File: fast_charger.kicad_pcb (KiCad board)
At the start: 2 copper layers, 71.1 x 38.7 mm, 47 parts, among them J1 Screw_Terminal_01x02, J2 USB_A, J3 AVR-ISP-6, J4 Conn_02x08_Odd_Even, J5 Conn_02x03_Odd_Even, Q1 PJD25N03, Q2 PJD25N03, U1 CHY100, U2 IRS10752LVBF, U3 ATtiny404-SS, U4 AP7375, U5 AP7375, U6 INA180A4

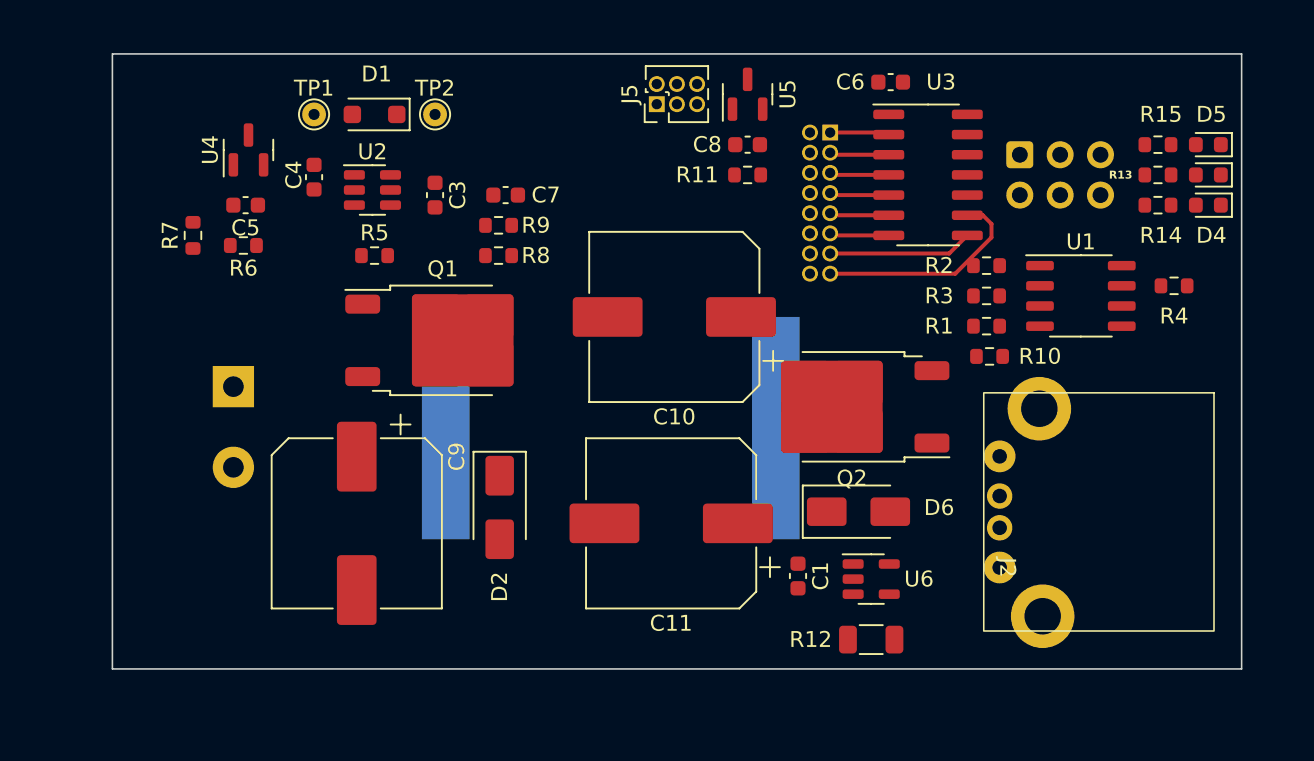
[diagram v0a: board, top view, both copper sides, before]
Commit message: Completed routing
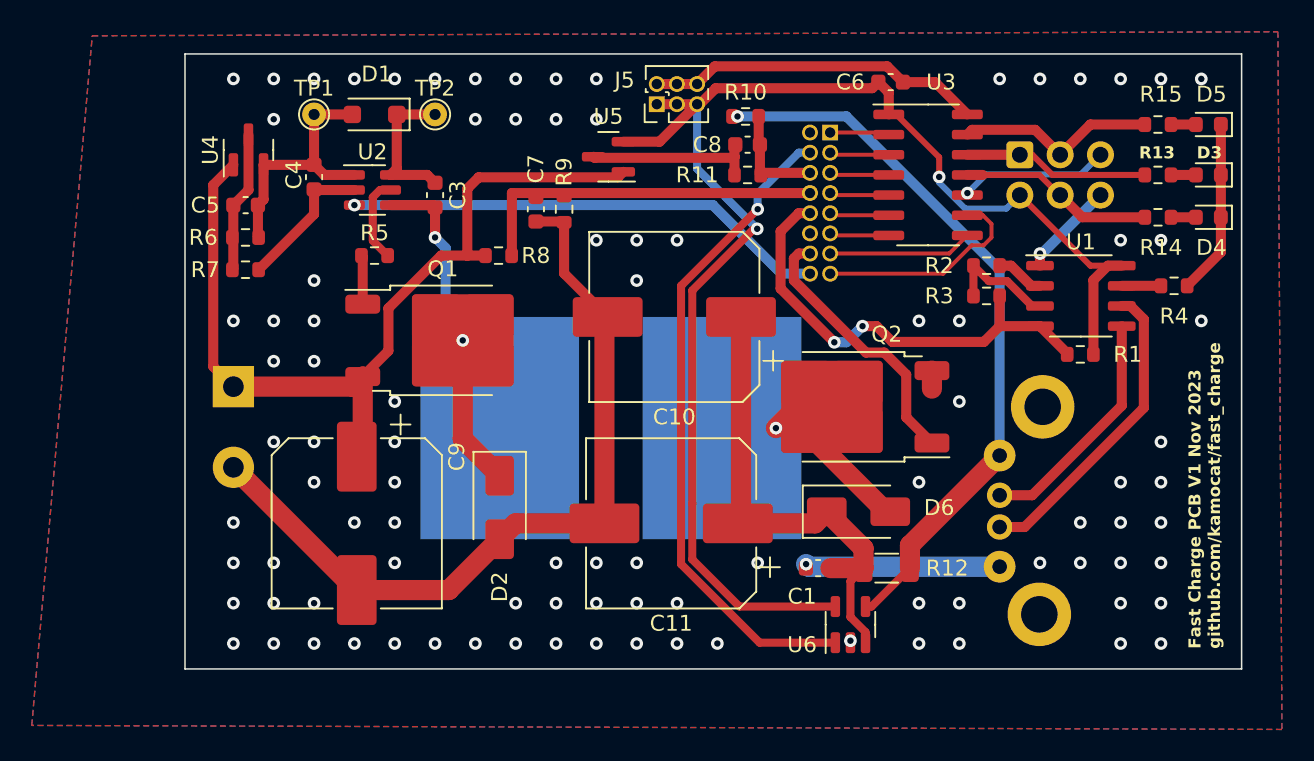
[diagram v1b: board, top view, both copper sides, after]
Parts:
- J2: moved to B.Cu
- moved R10 21.6 mm to (94.5, 55.4), turned to 0 degrees
- moved U5 9.61 mm to (85.9, 57.9), turned to 180 degrees
- moved J2 7.05 mm to (110.5, 76.7), turned to 90 degrees
- moved R1 6.17 mm to (115.6, 70.4), turned to 0 degrees
- moved R12 4.61 mm to (103.4, 83.8), turned to 0 degrees
- moved R9 4.25 mm to (83.1, 61.2), turned to -90 degrees
- moved R7 3.95 mm to (63.0, 65.0), turned to 0 degrees
- moved U6 3.15 mm to (101.1, 87.4), turned to 90 degrees
- moved C7 2.10 mm to (81.3, 61.2), turned to -90 degrees
- moved C1 1.36 mm to (99.1, 83.8), turned to 180 degrees
- moved D5 1.27 mm to (123.6, 55.9)
- moved R15 1.27 mm to (120.5, 55.9)
- moved D4 0.76 mm to (123.6, 61.7)
- moved R14 0.76 mm to (120.5, 61.7)
- moved R6 0.52 mm to (63.0, 63.0)
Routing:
- net GND: track 0.00 -> 133.0 mm, vias 0 -> 96
- net +5V: track 0.00 -> 91.9 mm, vias 0 -> 2
- net VDD: track 0.00 -> 55.6 mm
- net VBUS: track 0.00 -> 46.1 mm, vias 0 -> 1
- net /ILOAD: track 0.00 -> 41.5 mm, vias 0 -> 1
- net /VSW: track 0.00 -> 32.5 mm, vias 0 -> 2
- net Net-(D6-K): track 0.00 -> 31.0 mm
- net /PWM: track 0.00 -> 30.5 mm, vias 0 -> 1
- net /REQ_V: track 0.00 -> 29.3 mm, vias 0 -> 2
- net Net-(J4-Pin_8): track 0.00 -> 22.7 mm
- net Net-(J2-D+): track 0.00 -> 19.5 mm
- net /PWM2: track 0.00 -> 17.0 mm
- net Net-(D1-A): track 0.00 -> 16.4 mm
- net Net-(J2-D-): track 0.00 -> 15.0 mm
- net /MOSI: track 0.00 -> 13.3 mm
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- added copper zone on B.Cu, net GND
- added copper zone on F.Cu, net GND
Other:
- board size 71.1 x 38.7 mm -> 66.5 x 38.7 mm
- board text added: "Fast Charge PCB V1 Nov 2023 github.com/kamocat/fast_charge"

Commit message: V1 complete. PCB and parts ordered
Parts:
- D1: value SBM54 -> 1N4148W; footprint Diode_SMD:D_SOD-123F -> Diode_SMD:D_SOD-123
- moved R14 0.26 mm to (120.4, 62.0)
- moved D4 0.26 mm to (123.7, 62.0)
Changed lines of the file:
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@@
     (property "ki_keywords" "test point tp")
     (attr exclude_from_pos_files)
-    (fp_text reference "TP2" (at 0 -1.648) (layer "F.SilkS")
+    (fp_text reference "TP2" (at 2.54 -0.635) (layer "F.SilkS")
         (effects (font (size 1 1) (thickness 0.15)))
     )
@@
     (property "ki_keywords" "50mA LDO Regulator Fixed Positive")
     (attr smd)
-    (fp_text reference "U5" (at 0 2.54) (layer "F.SilkS")
+    (fp_text reference "U5" (at -0.508 2.54) (layer "F.SilkS")
         (effects (font (size 1 1) (thickness 0.15)))
     )
@@
     (property "ki_keywords" "transistor NMOS N-MOS N-MOSFET")
     (attr smd)
-    (fp_text reference "Q2" (at -2.193 4.572) (layer "F.SilkS")
+    (fp_text reference "Q2" (at -5.241 0) (layer "F.SilkS")
         (effects (font (size 1 1) (thickness 0.15)))
     )
@@
   )
   (footprint "Diode_SMD:D_0603_1608Metric" (layer "F.Cu")
-    (at 123.635 61.722 180)
+    (at 123.698 61.976 180)
     (descr "Diode SMD 0603 (1608 Metric), square (rectangular) end terminal, IPC_7351 nominal, (Body size source: http://www.tortai-tech.com/upload/download/2011102023233369053.pdf), generated with kicad-footprint-generator")
     (tags "diode")
@@
     (property "ki_keywords" "LED diode")
     (attr smd)
-    (fp_text reference "D4" (at -0.19 -1.905) (layer "F.SilkS")
-        (effects (font (size 1 1) (thickness 0.15)))
+    (fp_text reference "D4" (at -0.317 1.27) (layer "F.SilkS")
+        (effects (font (size 0.762 0.762) (thickness 0.127) bold))
     )
     (fp_text value "YEL" (at 0 1.43) (layer "F.Fab")
@@
     (property "ki_keywords" "test point tp")
     (attr exclude_from_pos_files)
-    (fp_text reference "TP1" (at 0 -1.648) (layer "F.SilkS")
+    (fp_text reference "TP1" (at -2.54 -0.635) (layer "F.SilkS")
         (effects (font (size 1 1) (thickness 0.15)))
     )
@@
   )
   (footprint "Resistor_SMD:R_0603_1608Metric" (layer "F.Cu")
-    (at 120.46 61.722)
+    (at 120.396 61.976)
     (descr "Resistor SMD 0603 (1608 Metric), square (rectangular) end terminal, IPC_7351 nominal, (Body size source: IPC-SM-782 page 72, https://www.pcb-3d.com/wordpress/wp-content/uploads/ipc-sm-782a_amendment_1_and_2.pdf), generated with kicad-footprint-generator")
     (tags "resistor")
@@
     (property "ki_keywords" "R res resistor")
     (attr smd)
-    (fp_text reference "R14" (at 0.19 1.905) (layer "F.SilkS")
-        (effects (font (size 1 1) (thickness 0.15)))
+    (fp_text reference "R14" (at -0.064 -1.27) (layer "F.SilkS")
+        (effects (font (size 0.762 0.762) (thickness 0.127) bold))
     )
     (fp_text value "1k" (at 0 1.43) (layer "F.Fab")
@@
     )
   )
-  (footprint "Diode_SMD:D_SOD-123F" (layer "F.Cu")
+  (footprint "Diode_SMD:D_SOD-123" (layer "F.Cu")
     (at 71.12 55.245 180)
-    (descr "D_SOD-123F")
-    (tags "D_SOD-123F")
+    (descr "SOD-123")
+    (tags "SOD-123")
     (property "Sheetfile" "fast_charger.kicad_sch")
     (property "Sheetname" "")
@@
     (property "ki_keywords" "diode Schottky")
     (attr smd)
-    (fp_text reference "D1" (at -0.127 2.54 180) (layer "F.SilkS")
-        (effects (font (size 1 1) (thickness 0.15)))
-    )
-    (fp_text value "SBM54" (at 0 2.1 180) (layer "F.Fab")
-        (effects (font (size 1 1) (thickness 0.15)))
-    )
-    (fp_text user "${REFERENCE}" (at -0.127 -1.905 180) (layer "F.Fab")
-        (effects (font (size 1 1) (thickness 0.15)))
-    )
-    (fp_line (start -2.21 -1) (end -2.21 1)
-      (stroke (width 0.12) (type solid)) (layer "F.SilkS"))
-    (fp_line (start -2.21 -1) (end 1.65 -1)
-      (stroke (width 0.12) (type solid)) (layer "F.SilkS"))
-    (fp_line (start -2.21 1) (end 1.65 1)
-      (stroke (width 0.12) (type solid)) (layer "F.SilkS"))
-    (fp_line (start -2.2 -1.15) (end -2.2 1.15)
-      (stroke (width 0.05) (type solid)) (layer "F.CrtYd"))
-    (fp_line (start -2.2 -1.15) (end 2.2 -1.15)
-      (stroke (width 0.05) (type solid)) (layer "F.CrtYd"))
-    (fp_line (start 2.2 -1.15) (end 2.2 1.15)
-      (stroke (width 0.05) (type solid)) (layer "F.CrtYd"))
-    (fp_line (start 2.2 1.15) (end -2.2 1.15)
+    (fp_text reference "D1" (at 0 1.905 180) (layer "F.SilkS")
+        (effects (font (size 1 1) (thickness 0.15)))
+    )
+    (fp_text value "1N4148W" (at 0 2.1 180) (layer "F.Fab")
+        (effects (font (size 1 1) (thickness 0.15)))
+    )
+    (fp_text user "${REFERENCE}" (at 0 -2 180) (layer "F.Fab")
+        (effects (font (size 1 1) (thickness 0.15)))
+    )
+    (fp_line (start -2.36 -1) (end -2.36 1)
+      (stroke (width 0.12) (type solid)) (layer "F.SilkS"))
+    (fp_line (start -2.36 -1) (end 1.65 -1)
+      (stroke (width 0.12) (type solid)) (layer "F.SilkS"))
+    (fp_line (start -2.36 1) (end 1.65 1)
+      (stroke (width 0.12) (type solid)) (layer "F.SilkS"))
+    (fp_line (start -2.35 -1.15) (end -2.35 1.15)
+      (stroke (width 0.05) (type solid)) (layer "F.CrtYd"))
+    (fp_line (start -2.35 -1.15) (end 2.35 -1.15)
+      (stroke (width 0.05) (type solid)) (layer "F.CrtYd"))
+    (fp_line (start 2.35 -1.15) (end 2.35 1.15)
+      (stroke (width 0.05) (type solid)) (layer "F.CrtYd"))
+    (fp_line (start 2.35 1.15) (end -2.35 1.15)
       (stroke (width 0.05) (type solid)) (layer "F.CrtYd"))
     (fp_line (start -1.4 -0.9) (end 1.4 -0.9)
@@
     (fp_line (start 1.4 0.9) (end -1.4 0.9)
       (stroke (width 0.1) (type solid)) (layer "F.Fab"))
-    (pad "1" smd roundrect (at -1.4 0 180) (size 1.1 1.1) (layers "F.Cu" "F.Paste" "F.Mask") (roundrect_rratio 0.2272727273)
+    (pad "1" smd roundrect (at -1.65 0 180) (size 0.9 1.2) (layers "F.Cu" "F.Paste" "F.Mask") (roundrect_rratio 0.25)
       (net 2 "Net-(D1-K)") (pinfunction "K") (pintype "passive"))
-    (pad "2" smd roundrect (at 1.4 0 180) (size 1.1 1.1) (layers "F.Cu" "F.Paste" "F.Mask") (roundrect_rratio 0.2272727273)
+    (pad "2" smd roundrect (at 1.65 0 180) (size 0.9 1.2) (layers "F.Cu" "F.Paste" "F.Mask") (roundrect_rratio 0.25)
       (net 4 "Net-(D1-A)") (pinfunction "A") (pintype "passive"))
-    (model "${KICAD6_3DMODEL_DIR}/Diode_SMD.3dshapes/D_SOD-123F.wrl"
+    (model "${KICAD6_3DMODEL_DIR}/Diode_SMD.3dshapes/D_SOD-123.wrl"
       (offset (xyz 0 0 0))
       (scale (xyz 1 1 1))
@@
     (property "ki_keywords" "R res resistor")
     (attr smd)
-    (fp_text reference "R1" (at 2.985 0) (layer "F.SilkS")
+    (fp_text reference "R1" (at 2.54 0.508) (layer "F.SilkS")
         (effects (font (size 1 1) (thickness 0.15)))
     )
@@
     (property "ki_keywords" "LED diode")
     (attr smd)
-    (fp_text reference "D5" (at -0.19 1.905) (layer "F.SilkS")
-        (effects (font (size 1 1) (thickness 0.15)))
+    (fp_text reference "D5" (at -0.19 1.524) (layer "F.SilkS")
+        (effects (font (size 0.762 0.762) (thickness 0.127) bold))
     )
     (fp_text value "GRN" (at 0 1.43) (layer "F.Fab")
@@
     (property "ki_keywords" "capacitor cap")
     (attr smd)
-    (fp_text reference "C1" (at 1.016 -1.778) (layer "F.SilkS")
+    (fp_text reference "C1" (at 0.762 -1.27) (layer "F.SilkS")
         (effects (font (size 1 1) (thickness 0.15)))
     )
@@
     (property "ki_keywords" "R res resistor")
     (attr smd)
-    (fp_text reference "R15" (at 0.19 -1.905) (layer "F.SilkS")
-        (effects (font (size 1 1) (thickness 0.15)))
+    (fp_text reference "R15" (at -0.064 -1.524) (layer "F.SilkS")
+        (effects (font (size 0.762 0.762) (thickness 0.127) bold))
     )
     (fp_text value "1k" (at 0 1.43) (layer "F.Fab")
@@
     (property "ki_keywords" "R res resistor")
     (attr smd)
-    (fp_text reference "R4" (at 0 1.905) (layer "F.SilkS")
+    (fp_text reference "R4" (at 2.477 0) (layer "F.SilkS")
         (effects (font (size 1 1) (thickness 0.15)))
     )
@@
   (segment (start 78.105 64.135) (end 76.962 64.135) (width 0.635) (layer "F.Cu") (net 8))
   (segment (start 122.8475 59.055) (end 121.285 59.055) (width 0.635) (layer "F.Cu") (net 9))
-  (segment (start 122.8475 61.722) (end 121.285 61.722) (width 0.635) (layer "F.Cu") (net 10))
+  (segment (start 122.9105 61.976) (end 121.221 61.976) (width 0.635) (layer "F.Cu") (net 10))
   (segment (start 122.8475 55.88) (end 121.285 55.88) (width 0.635) (layer "F.Cu") (net 11))
   (segment (start 102.422 86.2385) (end 104.8405 83.82) (width 0.508) (layer "F.Cu") (net 12))
@@
   (segment (start 119.635 55.88) (end 116.205 55.88) (width 0.635) (layer "F.Cu") (net 16))
   (segment (start 108.455 59.055) (end 112.99401 59.055) (width 0.381) (layer "F.Cu") (net 17))
-  (segment (start 115.697 61.722) (end 114.3 60.325) (width 0.635) (layer "F.Cu") (net 17))
+  (segment (start 119.571 61.976) (end 115.951 61.976) (width 0.635) (layer "F.Cu") (net 17))
   (segment (start 112.99401 59.055) (end 114.26401 60.325) (width 0.381) (layer "F.Cu") (net 17))
   (segment (start 114.26401 60.325) (end 114.3 60.325) (width 0.381) (layer "F.Cu") (net 17))
   (segment (start 108.455 59.055) (end 109.429999 59.055) (width 0.635) (layer "F.Cu") (net 17))
-  (segment (start 119.635 61.722) (end 115.697 61.722) (width 0.635) (layer "F.Cu") (net 17))
+  (segment (start 115.951 61.976) (end 114.3 60.325) (width 0.635) (layer "F.Cu") (net 17))
   (segment (start 108.455 60.201) (end 108.458 60.198) (width 0.381) (layer "F.Cu") (net 18))
   (segment (start 108.455 60.325) (end 108.455 60.201) (width 0.381) (layer "F.Cu") (net 18))

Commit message: Too many issues. Moving to a simpler design
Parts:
- R6: value 100k -> 4.7k
- R7: value 200k -> 10k
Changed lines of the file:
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@@
         (effects (font (size 1 1) (thickness 0.15)))
     )
-    (fp_text value "TestPoint" (at 0 1.75) (layer "F.Fab")
-        (effects (font (size 1 1) (thickness 0.15)))
-    )
-    (fp_text user "${REFERENCE}" (at 0 -1.65) (layer "F.Fab")
+    (fp_text value "TestPoint" (at 0 1.75) (layer "F.Fab") hide
+        (effects (font (size 1 1) (thickness 0.15)))
+    )
+    (fp_text user "${REFERENCE}" (at 2.54 -0.635) (layer "F.Fab")
         (effects (font (size 1 1) (thickness 0.15)))
     )
@@
         (effects (font (size 1 1) (thickness 0.15)))
     )
-    (fp_text value "AP7375" (at 0 2.4 90) (layer "F.Fab")
+    (fp_text value "AP7375" (at 1.6025 -0.315 180) (layer "F.Fab")
         (effects (font (size 1 1) (thickness 0.15)))
     )
@@
         (effects (font (size 1 1) (thickness 0.15)))
     )
-    (fp_text value "400k" (at 0 1.43) (layer "F.Fab")
+    (fp_text value "400k" (at 0.127 -1.397) (layer "F.Fab")
         (effects (font (size 1 1) (thickness 0.15)))
     )
@@
         (effects (font (size 1 1) (thickness 0.15)))
     )
-    (fp_text value "Conn_02x03_Odd_Even" (at 0.635 4.235 90) (layer "F.Fab")
+    (fp_text value "Conn_02x03_Odd_Even" (at 4.435 1.91 180) (layer "F.Fab")
         (effects (font (size 1 1) (thickness 0.15)))
     )
@@
         (effects (font (size 1 1) (thickness 0.15)))
     )
-    (fp_text value "100k" (at 0 1.43) (layer "F.Fab")
+    (fp_text value "100k" (at 2.985 0) (layer "F.Fab")
         (effects (font (size 1 1) (thickness 0.15)))
     )
@@
         (effects (font (size 1 1) (thickness 0.15)))
     )
-    (fp_text value "20m" (at 0 1.82) (layer "F.Fab")
+    (fp_text value "20m" (at 3.937 0) (layer "F.Fab")
         (effects (font (size 1 1) (thickness 0.15)))
     )
@@
         (effects (font (size 1 1) (thickness 0.15)))
     )
-    (fp_text value "100k" (at 0 1.43 90) (layer "F.Fab")
+    (fp_text value "100k" (at -0.254 -1.397 90) (layer "F.Fab")
         (effects (font (size 1 1) (thickness 0.15)))
     )
@@
         (effects (font (size 1 1) (thickness 0.15)))
     )
-    (fp_text value "10n" (at 0 1.43) (layer "F.Fab")
+    (fp_text value "10n" (at -2.66 -0.505) (layer "F.Fab")
         (effects (font (size 1 1) (thickness 0.15)))
     )
@@
         (effects (font (size 1 1) (thickness 0.15)))
     )
-    (fp_text value "TestPoint" (at 0 1.75) (layer "F.Fab")
+    (fp_text value "TestPoint" (at 3.81 -2.54) (layer "F.Fab") hide
         (effects (font (size 1 1) (thickness 0.15)))
     )
@@
         (effects (font (size 1 1) (thickness 0.15)))
     )
-    (fp_text value "INA180A4" (at 0 2.4 90) (layer "F.Fab")
+    (fp_text value "INA180A4" (at -0.889 -2.667 90) (layer "F.Fab")
         (effects (font (size 1 1) (thickness 0.15)))
     )
@@
         (effects (font (size 1 1) (thickness 0.15)))
     )
-    (fp_text value "1N4148W" (at 0 2.1 180) (layer "F.Fab")
+    (fp_text value "1N4148W" (at -1.905 2.1 180) (layer "F.Fab")
         (effects (font (size 1 1) (thickness 0.15)))
     )
@@
         (effects (font (size 1 1) (thickness 0.15)))
     )
-    (fp_text value "400k" (at 0 1.43) (layer "F.Fab")
+    (fp_text value "400k" (at 3.175 0.127) (layer "F.Fab")
         (effects (font (size 1 1) (thickness 0.15)))
     )
@@
         (effects (font (size 1 1) (thickness 0.15)))
     )
-    (fp_text value "10n" (at 0 1.43) (layer "F.Fab")
+    (fp_text value "10n" (at 2.675 0) (layer "F.Fab")
         (effects (font (size 1 1) (thickness 0.15)))
     )
@@
         (effects (font (size 1 1) (thickness 0.15)))
     )
-    (fp_text value "CHY100" (at 0 3.4) (layer "F.Fab")
+    (fp_text value "CHY100" (at 0 -3.175) (layer "F.Fab")
         (effects (font (size 1 1) (thickness 0.15)))
     )
@@
         (effects (font (size 1 1) (thickness 0.15)))
     )
-    (fp_text value "100k" (at 0 1.43) (layer "F.Fab")
+    (fp_text value "100k" (at 2.54 0) (layer "F.Fab")
         (effects (font (size 1 1) (thickness 0.15)))
     )
@@
         (effects (font (size 1 1) (thickness 0.15)))
     )
-    (fp_text value "200k" (at 0 1.43) (layer "F.Fab")
+    (fp_text value "10k" (at 0 1.43) (layer "F.Fab")
         (effects (font (size 1 1) (thickness 0.15)))
     )
@@
         (effects (font (size 1 1) (thickness 0.15)))
     )
-    (fp_text value "10n" (at 0 1.43) (layer "F.Fab")
+    (fp_text value "10n" (at 2.54 0) (layer "F.Fab")
         (effects (font (size 1 1) (thickness 0.15)))
     )
@@
         (effects (font (size 1 1) (thickness 0.15)))
     )
-    (fp_text value "100k" (at 0 1.43) (layer "F.Fab")
+    (fp_text value "100k" (at -2.985 0) (layer "F.Fab")
         (effects (font (size 1 1) (thickness 0.15)))
     )
@@
         (effects (font (size 1 1) (thickness 0.15)))
     )
-    (fp_text value "SBM54" (at 0 2.6) (layer "F.Fab")
-        (effects (font (size 1 1) (thickness 0.15)))
-    )
-    (fp_text user "${REFERENCE}" (at 0 -2.5) (layer "F.Fab")
+    (fp_text value "SBM54" (at 3.175 -2.16) (layer "F.Fab")
+        (effects (font (size 1 1) (thickness 0.15)))
+    )
+    (fp_text user "${REFERENCE}" (at -1.27 -2.16) (layer "F.Fab")
         (effects (font (size 1 1) (thickness 0.15)))
     )
@@
         (effects (font (size 1 1) (thickness 0.15)))
     )
-    (fp_text value "100k" (at 0 1.43) (layer "F.Fab")
+    (fp_text value "4.7k" (at 2.667 0.127) (layer "F.Fab")
         (effects (font (size 1 1) (thickness 0.15)))
     )
@@
         (effects (font (size 1 1) (thickness 0.15)))
     )
-    (fp_text value "ATtiny404-SS" (at 0 5.28) (layer "F.Fab")
+    (fp_text value "ATtiny404-SS" (at 3.875 -5.08) (layer "F.Fab")
         (effects (font (size 1 1) (thickness 0.15)))
     )
@@
     (pts (xy 125.73 51.435) (xy 125.73 90.17))
     (height -5.715)
-    (gr_text "1525.0000 mils" (at 130.295 70.8025 90) (layer "User.1")
+    (gr_text "1.5250 in" (at 130.295 70.8025 90) (layer "User.1")
       (effects (font (size 1 1) (thickness 0.15)))
     )
@@
     (pts (xy 125.73 90.17) (xy 59.182 90.17))
     (height -6.35)
-    (gr_text "2620.0000 mils" (at 92.456 95.37) (layer "User.1")
+    (gr_text "2.6200 in" (at 92.456 95.37) (layer "User.1")
       (effects (font (size 1 1) (thickness 0.15)))
     )
